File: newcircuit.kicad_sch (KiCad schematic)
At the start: 3 parts

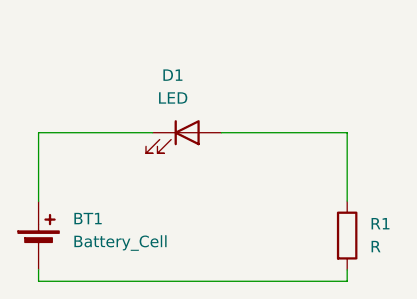
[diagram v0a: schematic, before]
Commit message: 2 led series
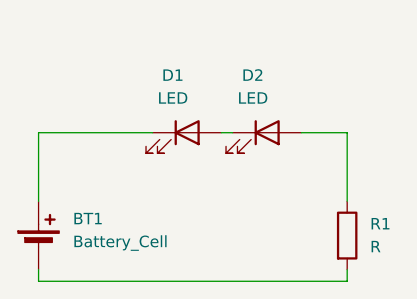
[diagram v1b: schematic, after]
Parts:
- added D2: LED, symbol Device:LED
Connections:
- net at D1.2 (A): now also D2.1 (K); no longer R1.1
- new net: D2.2 (A), R1.1
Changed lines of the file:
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@@
+	(wire
+		(pts
+			(xy 132.08 68.58) (xy 133.35 68.58)
+		)
+		(stroke
+			(width 0)
+			(type default)
+		)
+	)
 	(wire
 		(pts
@@
 	(wire
 		(pts
-			(xy 132.08 68.58) (xy 146.05 68.58)
-		)
-		(stroke
-			(width 0)
-			(type default)
-		)
-	)
-	(wire
-		(pts
 			(xy 111.76 85.09) (xy 111.76 83.82)
 		)
@@
 		(pts
 			(xy 146.05 83.82) (xy 146.05 85.09)
+		)
+		(stroke
+			(width 0)
+			(type default)
+		)
+	)
+	(wire
+		(pts
+			(xy 140.97 68.58) (xy 146.05 68.58)
 		)
 		(stroke
@@
 					(unit 1)
 				)
+			)
+		)
+	)
+	(symbol
+		(lib_id "Device:LED")
+		(at 137.16 68.58 0)
+		(unit 1)
+		(exclude_from_sim no)
+		(in_bom yes)
+		(on_board yes)
+		(dnp no)
+		(fields_autoplaced yes)
+		(property "Reference" "D2"
+			(at 135.5725 62.23 0)
+			(effects
+				(font
+					(size 1.27 1.27)
+				)
+			)
+		)
+		(property "Value" "LED"
+			(at 135.5725 64.77 0)
+			(effects
+				(font
+					(size 1.27 1.27)
+				)
+			)
+		)
+		(property "Footprint" ""
+			(at 137.16 68.58 0)
+			(effects
+				(font
+					(size 1.27 1.27)
+				)
+				(hide yes)
+			)
+		)
+		(property "Datasheet" "~"
+			(at 137.16 68.58 0)
+			(effects
+				(font
+					(size 1.27 1.27)
+				)
+				(hide yes)
+			)
+		)
+		(property "Description" "Light emitting diode"
+			(at 137.16 68.58 0)
+			(effects
+				(font
+					(size 1.27 1.27)
+				)
+				(hide yes)
+			)
+		)
+		(property "Sim.Pins" "1=K 2=A"
+			(at 137.16 68.58 0)
+			(effects
+				(font
+					(size 1.27 1.27)
+				)
+				(hide yes)
+			)
+		)
+		(pin "2"
+		)
+		(pin "1"
+		)
+		(instances
+			(project "newcircuit"
+				(path "/8b06aeeb-6994-498e-9631-778fb4ee0666"
+					(reference "D2")
+					(unit 1)
+				)

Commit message: 4 led with parallel
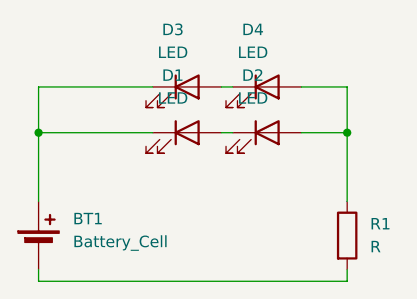
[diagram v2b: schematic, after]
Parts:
- added D3, D4: LED, symbol Device:LED
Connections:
- net at BT1.1 (+), D1.1 (K): now also D3.1 (K)
- net at D2.2 (A), R1.1: now also D4.2 (A)
- new net: D3.2 (A), D4.1 (K)
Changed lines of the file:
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@@
 	(generator_version "9.0")
 	(paper "A4")
+	(junction
+		(at 111.76 68.58)
+		(diameter 0)
+		(color 0 0 0 0)
+	)
+	(junction
+		(at 146.05 68.58)
+		(diameter 0)
+		(color 0 0 0 0)
+	)
+	(wire
+		(pts
+			(xy 132.08 63.5) (xy 133.35 63.5)
+		)
+		(stroke
+			(width 0)
+			(type default)
+		)
+	)
+	(wire
+		(pts
+			(xy 111.76 63.5) (xy 124.46 63.5)
+		)
+		(stroke
+			(width 0)
+			(type default)
+		)
+	)
+	(wire
+		(pts
+			(xy 146.05 85.09) (xy 111.76 85.09)
+		)
+		(stroke
+			(width 0)
+			(type default)
+		)
+	)
+	(wire
+		(pts
+			(xy 140.97 63.5) (xy 146.05 63.5)
+		)
+		(stroke
+			(width 0)
+			(type default)
+		)
+	)
+	(wire
+		(pts
+			(xy 146.05 63.5) (xy 146.05 68.58)
+		)
+		(stroke
+			(width 0)
+			(type default)
+		)
+	)
+	(wire
+		(pts
+			(xy 111.76 76.2) (xy 111.76 68.58)
+		)
+		(stroke
+			(width 0)
+			(type default)
+		)
+	)
+	(wire
+		(pts
+			(xy 146.05 68.58) (xy 146.05 76.2)
+		)
+		(stroke
+			(width 0)
+			(type default)
+		)
+	)
 	(wire
 		(pts
@@
 	(wire
 		(pts
-			(xy 146.05 85.09) (xy 111.76 85.09)
-		)
-		(stroke
-			(width 0)
-			(type default)
-		)
-	)
-	(wire
-		(pts
-			(xy 111.76 76.2) (xy 111.76 68.58)
-		)
-		(stroke
-			(width 0)
-			(type default)
-		)
-	)
-	(wire
-		(pts
-			(xy 146.05 68.58) (xy 146.05 76.2)
-		)
-		(stroke
-			(width 0)
-			(type default)
-		)
-	)
-	(wire
-		(pts
 			(xy 111.76 85.09) (xy 111.76 83.82)
 		)
@@
 		(pts
 			(xy 140.97 68.58) (xy 146.05 68.58)
+		)
+		(stroke
+			(width 0)
+			(type default)
+		)
+	)
+	(wire
+		(pts
+			(xy 111.76 63.5) (xy 111.76 68.58)
 		)
 		(stroke
@@
 					(unit 1)
 				)
+			)
+		)
+	)
+	(symbol
+		(lib_id "Device:LED")
+		(at 137.16 63.5 0)
+		(unit 1)
+		(exclude_from_sim no)
+		(in_bom yes)
+		(on_board yes)
+		(dnp no)
+		(fields_autoplaced yes)
+		(property "Reference" "D4"
+			(at 135.5725 57.15 0)
+			(effects
+				(font
+					(size 1.27 1.27)
+				)
+			)
+		)
+		(property "Value" "LED"
+			(at 135.5725 59.69 0)
+			(effects
+				(font
+					(size 1.27 1.27)
+				)
+			)
+		)
+		(property "Footprint" ""
+			(at 137.16 63.5 0)
+			(effects
+				(font
+					(size 1.27 1.27)
+				)
+				(hide yes)
+			)
+		)
+		(property "Datasheet" "~"
+			(at 137.16 63.5 0)
+			(effects
+				(font
+					(size 1.27 1.27)
+				)
+				(hide yes)
+			)
+		)
+		(property "Description" "Light emitting diode"
+			(at 137.16 63.5 0)
+			(effects
+				(font
+					(size 1.27 1.27)
+				)
+				(hide yes)
+			)
+		)
+		(property "Sim.Pins" "1=K 2=A"
+			(at 137.16 63.5 0)
+			(effects
+				(font
+					(size 1.27 1.27)
+				)
+				(hide yes)
+			)
+		)
+		(pin "2"
+		)
+		(pin "1"
+		)
+		(instances
+			(project "newcircuit"
+				(path "/8b06aeeb-6994-498e-9631-778fb4ee0666"
+					(reference "D4")
+					(unit 1)
+				)
+			)
+		)
+	)
+	(symbol
+		(lib_id "Device:LED")
+		(at 128.27 63.5 0)
+		(unit 1)
+		(exclude_from_sim no)
+		(in_bom yes)
+		(on_board yes)
+		(dnp no)
+		(fields_autoplaced yes)
+		(property "Reference" "D3"
+			(at 126.6825 57.15 0)
+			(effects
+				(font
+					(size 1.27 1.27)
+				)
+			)
+		)
+		(property "Value" "LED"
+			(at 126.6825 59.69 0)
+			(effects
+				(font
+					(size 1.27 1.27)
+				)
+			)
+		)
+		(property "Footprint" ""
+			(at 128.27 63.5 0)
+			(effects
+				(font
+					(size 1.27 1.27)
+				)
+				(hide yes)
+			)
+		)
+		(property "Datasheet" "~"
+			(at 128.27 63.5 0)
+			(effects
+				(font
+					(size 1.27 1.27)
+				)
+				(hide yes)
+			)
+		)
+		(property "Description" "Light emitting diode"
+			(at 128.27 63.5 0)
+			(effects
+				(font
+					(size 1.27 1.27)
+				)
+				(hide yes)
+			)
+		)
+		(property "Sim.Pins" "1=K 2=A"
+			(at 128.27 63.5 0)
+			(effects
+				(font
+					(size 1.27 1.27)
+				)
+				(hide yes)
+			)
+		)
+		(pin "2"
+		)
+		(pin "1"
+		)
+		(instances
+			(project "newcircuit"
+				(path "/8b06aeeb-6994-498e-9631-778fb4ee0666"
+					(reference "D3")
+					(unit 1)
+				)
